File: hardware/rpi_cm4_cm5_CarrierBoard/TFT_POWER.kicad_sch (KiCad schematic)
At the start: 86 parts, among them Q14 2N7002, Q15 2N7002, Q16 BCP56-16, Q17 ISP75DP06LMXTSA1, Q18 MMBT3904-7-F, U24 MAX16928CGUP, U25 TPS79901DRVR, U26 TPS61169DCKR, U27 AP22913W6-7

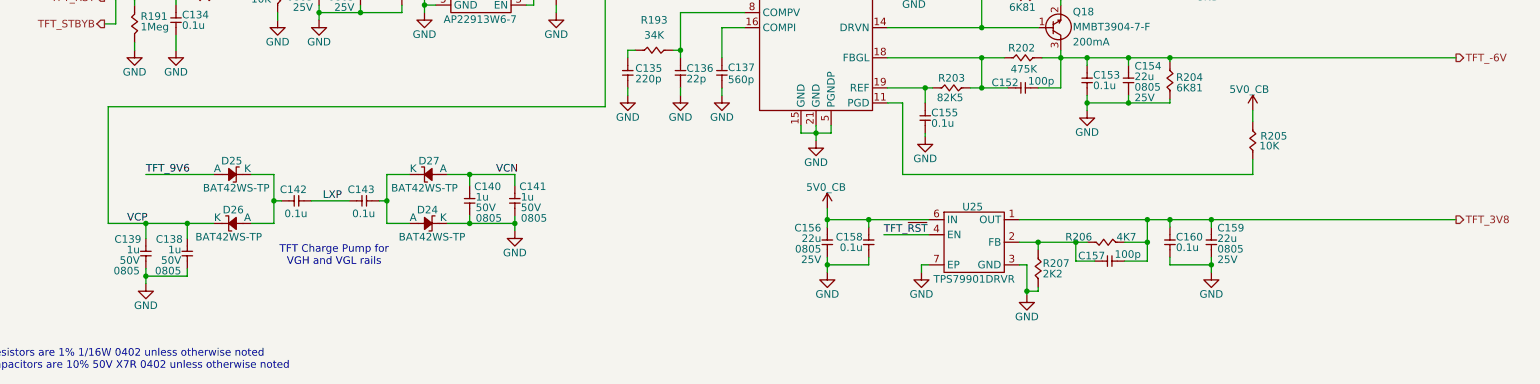
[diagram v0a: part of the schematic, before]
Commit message: Add power-up and power kill sequences Modify schematics to add net classes for DiffPairs
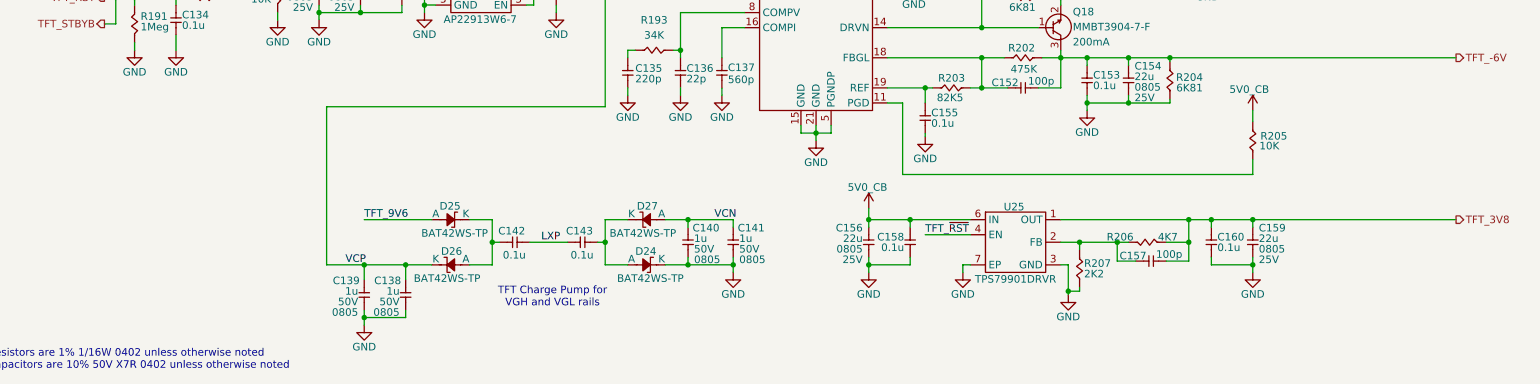
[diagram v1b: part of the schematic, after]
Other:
- moved on the sheet: C138, C139, C140, C141, C142, C143, C156, C157, C158, C159, C160, D24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

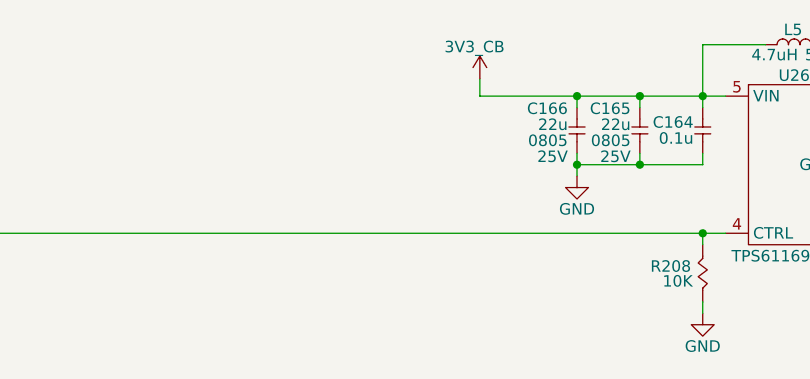
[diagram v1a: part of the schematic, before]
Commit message: Add preliminary BOM and preliminary .pdf schmematics Add BOM option for I2C control of ILI2132A for CapTouch HMI Add BOM options and DNP / 0R resistors for CM4 - CM5 build options
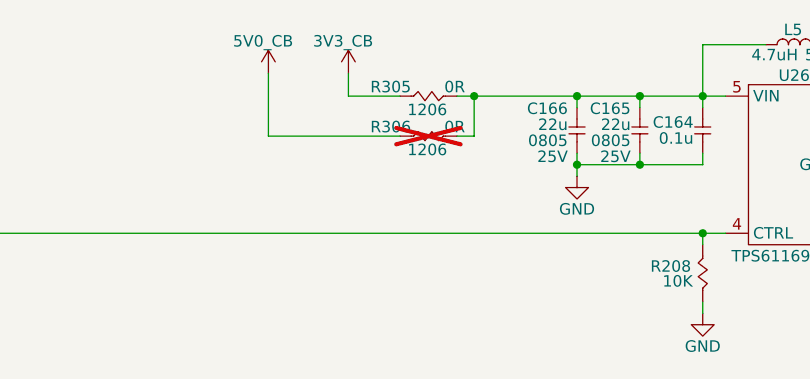
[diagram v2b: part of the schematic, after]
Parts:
- added R305, R306: 0R, footprint:RES_1206, symbol KicadCompDb:Resistors/RES_SMT_00022
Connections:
- net 3V3_CB: now also R305.1; no longer C164.2, C165.2, C166.2, L5.1, U26.5 (VIN)
- net 5V0_CB: now also R306.1
- new net: C164.2, C165.2, C166.2, L5.1, R305.2, R306.2, U26.5 (VIN)

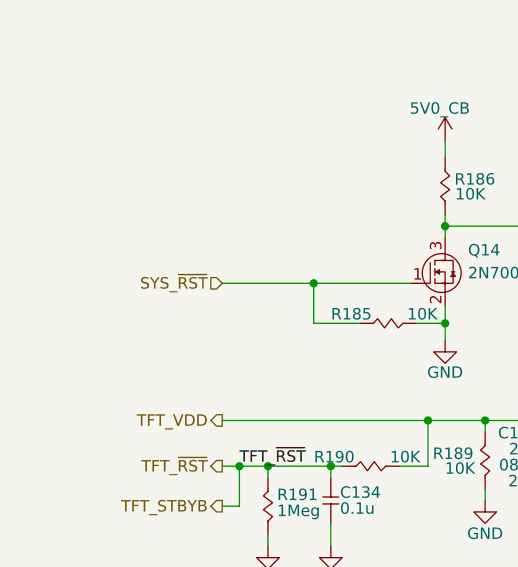
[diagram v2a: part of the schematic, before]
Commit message: Added power input protection & filter Added dedicated QWIIC connector on RPI CMx I2C6 bus Adjusted power table and PinMux Updated schematics accordingly
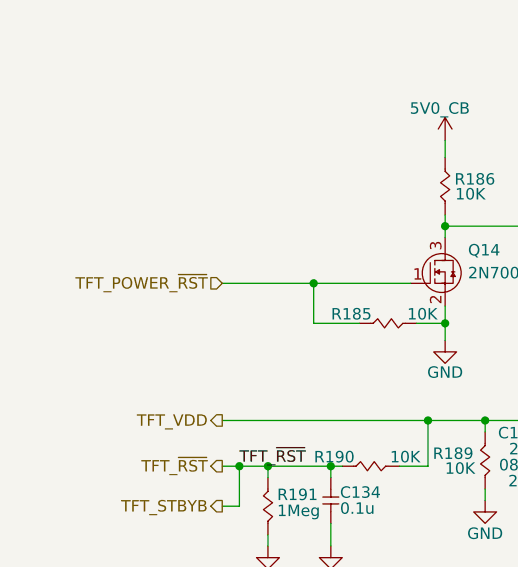
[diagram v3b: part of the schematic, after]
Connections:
- net SYS_~{RST} renamed TFT_POWER_~{RST}
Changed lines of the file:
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@@
 		)
 	)
-	(hierarchical_label "SYS_~{RST}"
+	(hierarchical_label "TFT_POWER_~{RST}"
 		(shape input)
 		(at 32.385 89.535 180)

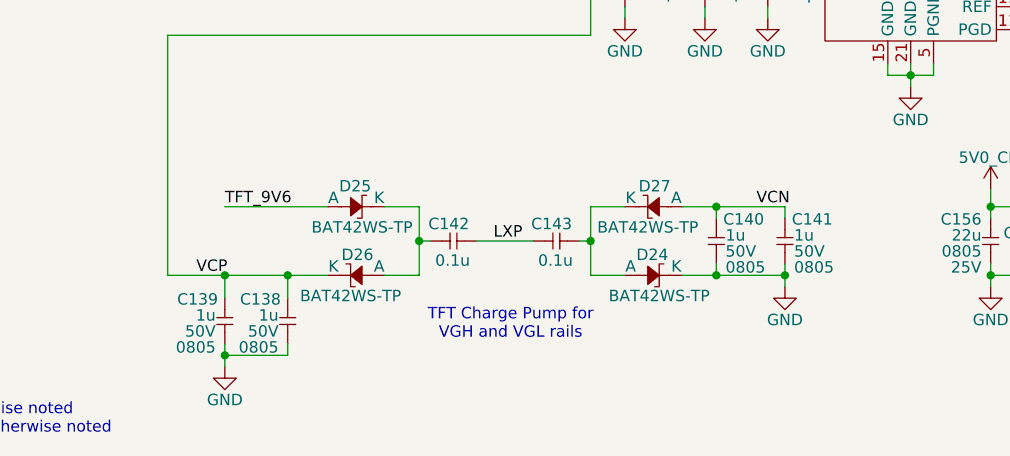
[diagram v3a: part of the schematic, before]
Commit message: Update preliminary placement, update DNP, regen BOM + Preliminary schematics
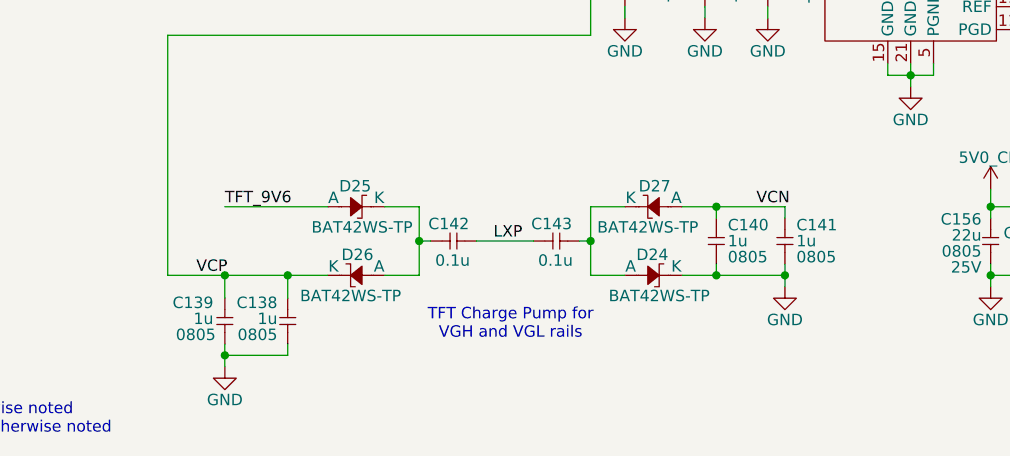
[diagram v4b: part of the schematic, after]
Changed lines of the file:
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@@
 		(dnp no)
 		(property "Reference" "C140"
-			(at 131.572 148.717 90)
+			(at 132.08 149.352 90)
 			(effects
 				(font
@@
 		)
 		(property "Value" "1u"
-			(at 131.826 150.495 90)
+			(at 132.08 151.13 90)
 			(effects
 				(font
@@
 		)
 		(property "Package" "0805"
-			(at 131.826 154.051 90)
+			(at 132.08 152.908 90)
 			(effects
 				(font
@@
 				)
 				(justify right)
+				(hide yes)
 			)
 		)
@@
 		(dnp no)
 		(property "Reference" "C138"
-			(at 82.423 157.607 90)
+			(at 82.042 157.988 90)
 			(effects
 				(font
@@
 		)
 		(property "Value" "1u"
-			(at 82.169 159.385 90)
+			(at 82.042 159.766 90)
 			(effects
 				(font
@@
 		)
 		(property "Package" "0805"
-			(at 82.169 162.941 90)
+			(at 82.042 161.544 90)
 			(effects
 				(font
@@
 				)
 				(justify right)
+				(hide yes)
 			)
 		)
@@
 		(dnp no)
 		(property "Reference" "C141"
-			(at 139.192 148.717 90)
+			(at 139.7 149.352 90)
 			(effects
 				(font
@@
 		)
 		(property "Value" "1u"
-			(at 139.446 150.495 90)
+			(at 139.7 151.13 90)
 			(effects
 				(font
@@
 		)
 		(property "Package" "0805"
-			(at 139.446 154.051 90)
+			(at 139.7 152.908 90)
 			(effects
 				(font
@@
 				)
 				(justify right)
+				(hide yes)
 			)
 		)
@@
 		(dnp no)
 		(property "Reference" "C139"
-			(at 75.438 157.607 90)
+			(at 74.93 157.988 90)
 			(effects
 				(font
@@
 		)
 		(property "Value" "1u"
-			(at 75.184 159.385 90)
+			(at 74.93 159.766 90)
 			(effects
 				(font
@@
 		)
 		(property "Package" "0805"
-			(at 75.184 162.941 90)
+			(at 75.184 161.544 90)
 			(effects
 				(font
@@
 				)
 				(justify right)
+				(hide yes)
 			)
 		)

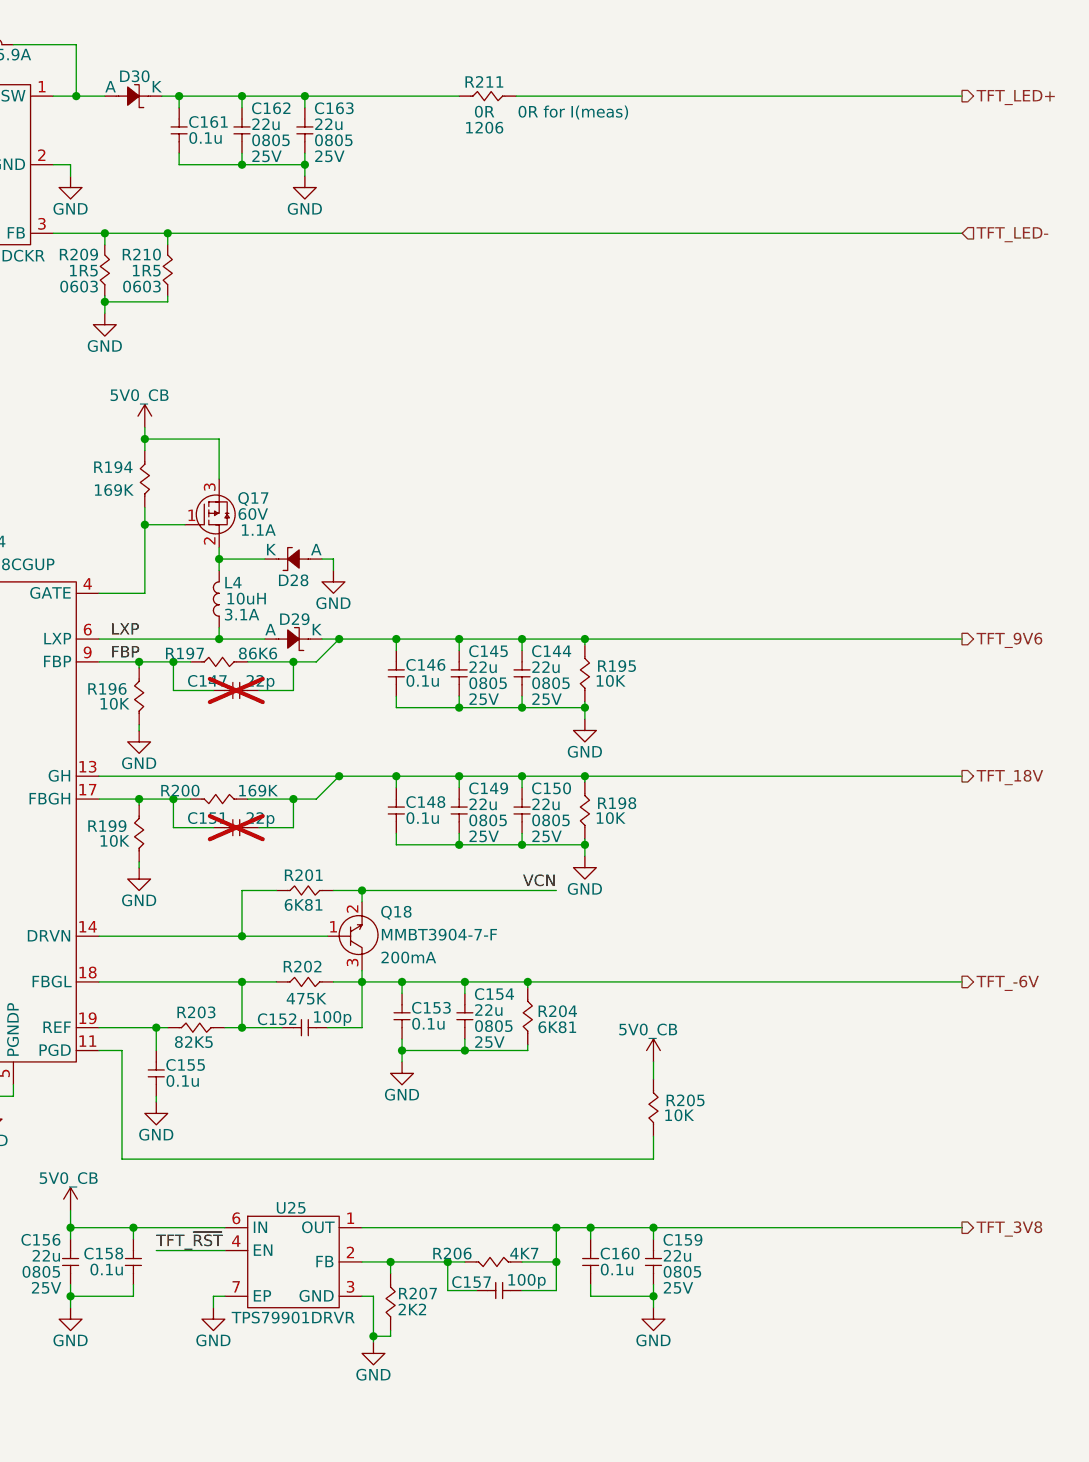
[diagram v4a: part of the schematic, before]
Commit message: Update PCB design rules for outer layers differential pairs Update preliminary component placement Update schematics based on PCB placement & remove duplicata / unnecessary components Update design notes and power table
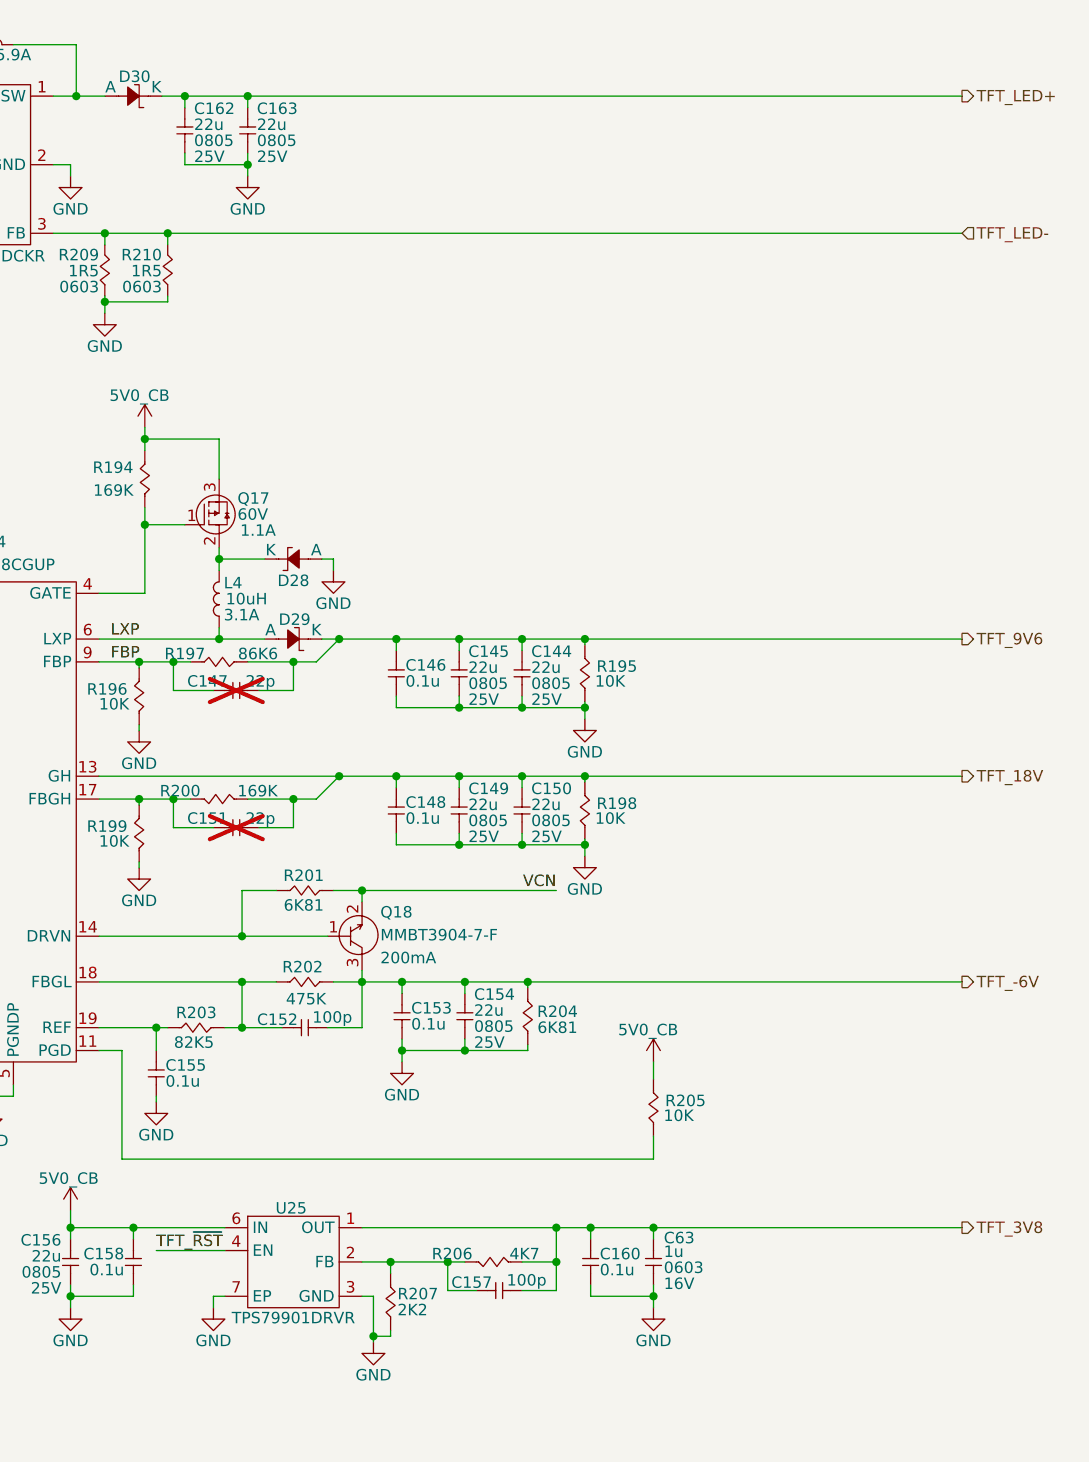
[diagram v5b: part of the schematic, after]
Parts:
- removed C159: 22u, footprint:CAP_NONPOL_0805, symbol KicadCompDb:Capacitors/CAP_CER_SMT_00011
- removed C161: 0.1u, footprint:CAP_NONPOL_0402, symbol KicadCompDb:Capacitors/CAP_CER_SMT_00001
- removed R211: 0R, footprint:RES_1206, symbol KicadCompDb:Resistors/RES_SMT_00022
- added C63: 1u, footprint:CAP_NONPOL_0603, symbol KicadCompDb:Capacitors/CAP_CER_SMT_00015
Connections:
- net GND: now also C63.1
- net TFT_3V8: now also C63.2
- net TFT_LED+: now also C162.2, C163.2, D30.1 (K)
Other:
- note removed: "0R for I(meas)"
- moved on the sheet: C162, C163
